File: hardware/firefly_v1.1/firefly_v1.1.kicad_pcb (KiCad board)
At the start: 2 copper layers, 31.2 x 10.2 mm, 10 parts, among them J1 VCC, J2 Conn_01x04, J3 GND, Q1 IRLML6344, U1 MSP430G2231IN14

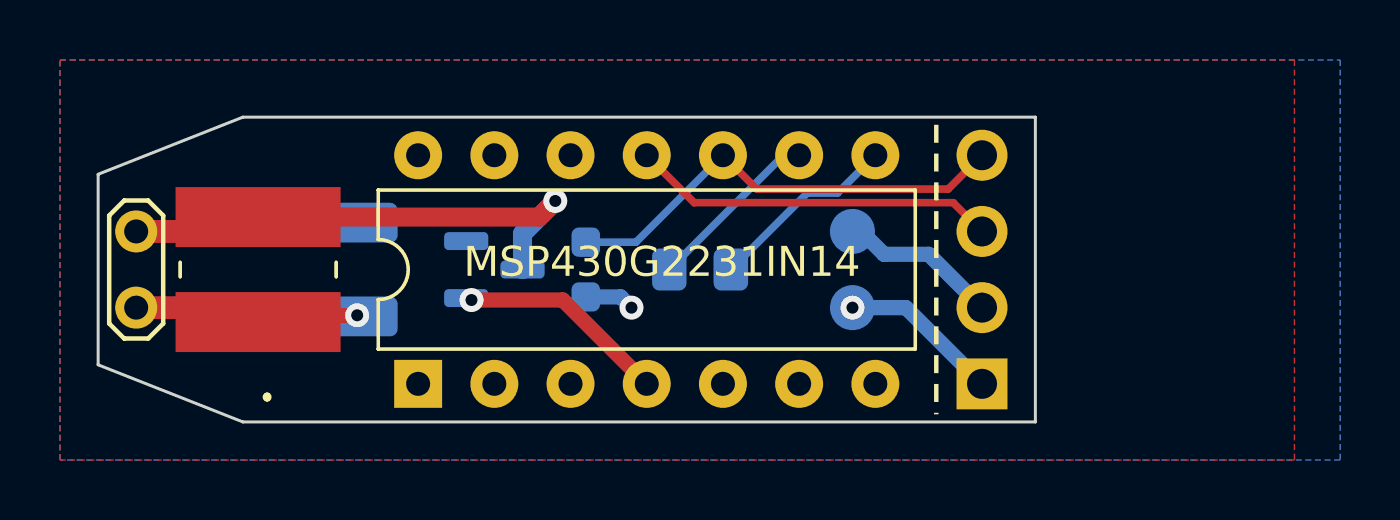
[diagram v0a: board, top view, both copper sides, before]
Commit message: Switch to footprint from curated global libs
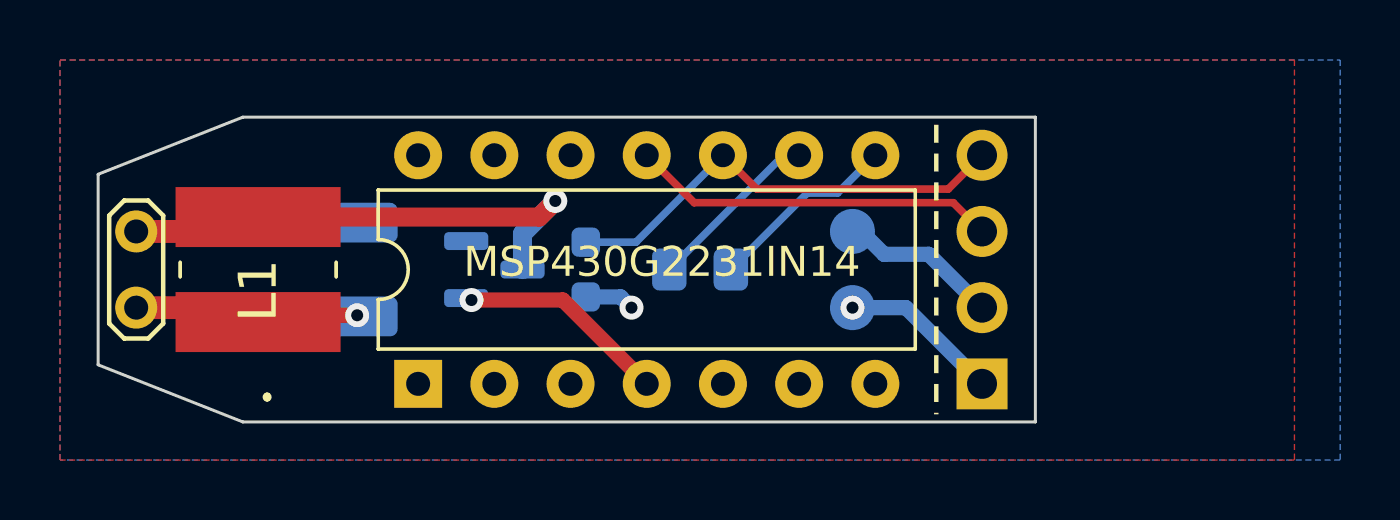
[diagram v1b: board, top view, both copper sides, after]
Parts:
- L1: footprint LIB_HM79M-20102LFTR:HM79M20102LFTR -> Inductor_SMD:L_HM79M20102LFTR
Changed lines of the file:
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@@
     )
   )
-  (footprint "LIB_HM79M-20102LFTR:HM79M20102LFTR" (layer "F.Cu")
+  (footprint "Inductor_SMD:L_HM79M20102LFTR" (layer "F.Cu")
     (at 139.7 94.742 90)
     (descr "HM79M-20102LFTR-2")
@@
     (property "ki_keywords" "simulation")
     (attr smd)
-    (fp_text reference "L1" (at -0.7 0 90) (layer "F.SilkS") hide
+    (fp_text reference "L1" (at -0.7 0 90) (layer "F.SilkS")
         (effects (font (size 1.27 1.27) (thickness 0.254)))
     )
